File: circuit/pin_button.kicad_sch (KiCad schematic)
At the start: 5 parts, among them SW1 select, SW2 start

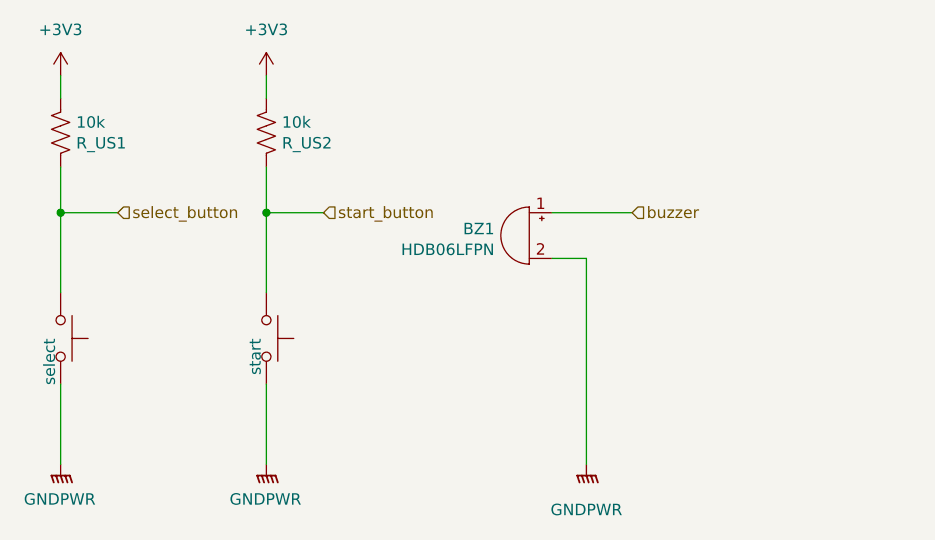
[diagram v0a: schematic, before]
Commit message: [update] update buzzer peripheral circuit
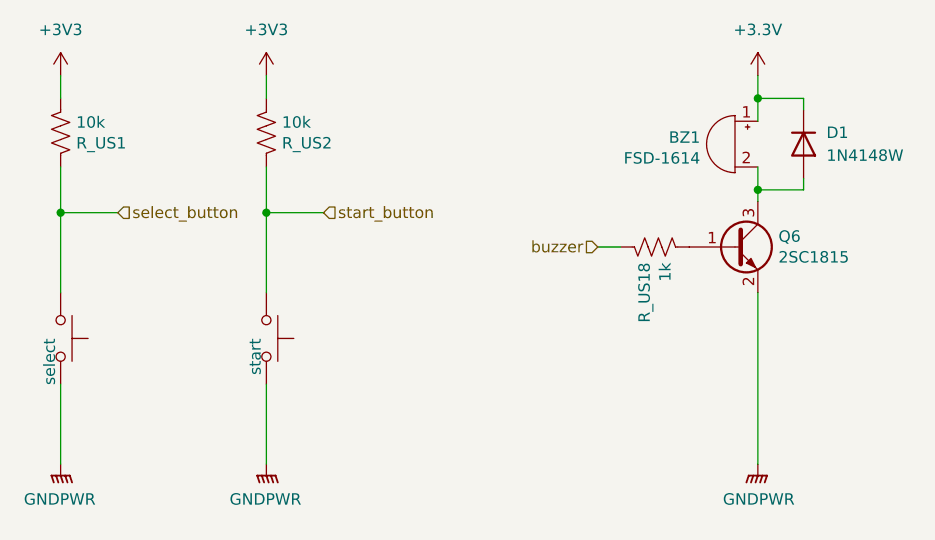
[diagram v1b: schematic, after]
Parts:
- added D1: 1N4148W, Diode_SMD:D_SOD-123, symbol Diode:1N4148W
- added Q6: 2SC1815, Package_TO_SOT_SMD:SOT-23, symbol Transistor_BJT:2SC1815
- added R_US18: 1k, Resistor_SMD:R_0805_2012Metric, symbol Device:R_US
- BZ1: value HDB06LFPN -> FSD-1614
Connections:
- net GNDPWR: now also Q6.2 (E); no longer BZ1.2 (+)
- net buzzer: now also R_US18.1; no longer BZ1.1 (-)
- new net: BZ1.2 (+), D1.2 (A), Q6.3 (C)
- new net: Q6.1 (B), R_US18.2
- new net +3.3V: BZ1.1 (-), D1.1 (K)
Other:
- moved on the sheet: BZ1

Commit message: [update] re-annotate symbols
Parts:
- renumbered Q6 to Q5, R_US1 to R_US16, R_US2 to R_US17, SW1 to SW2, SW2 to SW3
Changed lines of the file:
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@@
 		(dnp no)
 		(fields_autoplaced yes)
-		(property "Reference" "#PWR01"
+		(property "Reference" "#PWR018"
 			(at 116.84 73.66 0)
 			(effects
@@
 			(project "gen3"
 				(path "/4fc99a72-ed0b-4d28-88d8-569af68d8cfc/a6a603d2-5a16-46d3-94ac-e9e8583c5e5b"
-					(reference "#PWR01")
+					(reference "#PWR018")
 					(unit 1)
 				)
@@
 		(on_board yes)
 		(dnp no)
-		(property "Reference" "#PWR03"
+		(property "Reference" "#PWR021"
 			(at 116.84 118.11 0)
 			(effects
@@
 			(project "gen3"
 				(path "/4fc99a72-ed0b-4d28-88d8-569af68d8cfc/a6a603d2-5a16-46d3-94ac-e9e8583c5e5b"
-					(reference "#PWR03")
+					(reference "#PWR021")
 					(unit 1)
 				)
@@
 		(on_board yes)
 		(dnp no)
-		(property "Reference" "#PWR04"
+		(property "Reference" "#PWR022"
 			(at 139.7 118.11 0)
 			(effects
@@
 			(project "gen3"
 				(path "/4fc99a72-ed0b-4d28-88d8-569af68d8cfc/a6a603d2-5a16-46d3-94ac-e9e8583c5e5b"
-					(reference "#PWR04")
+					(reference "#PWR022")
 					(unit 1)
 				)
@@
 		(on_board yes)
 		(dnp no)
-		(property "Reference" "R_US1"
+		(property "Reference" "R_US16"
 			(at 118.5672 77.3684 0)
 			(effects
@@
 			(project "gen3"
 				(path "/4fc99a72-ed0b-4d28-88d8-569af68d8cfc/a6a603d2-5a16-46d3-94ac-e9e8583c5e5b"
-					(reference "R_US1")
+					(reference "R_US16")
 					(unit 1)
 				)
@@
 		(dnp no)
 		(fields_autoplaced yes)
-		(property "Reference" "#PWR02"
+		(property "Reference" "#PWR019"
 			(at 139.7 73.66 0)
 			(effects
@@
 			(project "gen3"
 				(path "/4fc99a72-ed0b-4d28-88d8-569af68d8cfc/a6a603d2-5a16-46d3-94ac-e9e8583c5e5b"
-					(reference "#PWR02")
+					(reference "#PWR019")
 					(unit 1)
 				)
@@
 		(on_board yes)
 		(dnp no)
-		(property "Reference" "Q6"
+		(property "Reference" "Q5"
 			(at 196.596 87.7316 0)
 			(effects
@@
 			(project "gen3"
 				(path "/4fc99a72-ed0b-4d28-88d8-569af68d8cfc/a6a603d2-5a16-46d3-94ac-e9e8583c5e5b"
-					(reference "Q6")
+					(reference "Q5")
 					(unit 1)
 				)
@@
 		(on_board yes)
 		(dnp no)
-		(property "Reference" "#PWR024"
+		(property "Reference" "#PWR023"
 			(at 194.31 118.11 0)
 			(effects
@@
 			(project "gen3"
 				(path "/4fc99a72-ed0b-4d28-88d8-569af68d8cfc/a6a603d2-5a16-46d3-94ac-e9e8583c5e5b"
-					(reference "#PWR024")
+					(reference "#PWR023")
 					(unit 1)
 				)
@@
 		(on_board yes)
 		(dnp no)
-		(property "Reference" "SW2"
+		(property "Reference" "SW3"
 			(at 146.939 99.06 0)
 			(effects
@@
 			(project "gen3"
 				(path "/4fc99a72-ed0b-4d28-88d8-569af68d8cfc/a6a603d2-5a16-46d3-94ac-e9e8583c5e5b"
-					(reference "SW2")
+					(reference "SW3")
 					(unit 1)
 				)
@@
 		(on_board yes)
 		(dnp no)
-		(property "Reference" "R_US2"
+		(property "Reference" "R_US17"
 			(at 141.4272 77.3684 0)
 			(effects
@@
 			(project "gen3"
 				(path "/4fc99a72-ed0b-4d28-88d8-569af68d8cfc/a6a603d2-5a16-46d3-94ac-e9e8583c5e5b"
-					(reference "R_US2")
+					(reference "R_US17")
 					(unit 1)
 				)
@@
 		(dnp no)
 		(fields_autoplaced yes)
-		(property "Reference" "#PWR05"
+		(property "Reference" "#PWR020"
 			(at 194.31 73.66 0)
 			(effects
@@
 			(project ""
 				(path "/4fc99a72-ed0b-4d28-88d8-569af68d8cfc/a6a603d2-5a16-46d3-94ac-e9e8583c5e5b"
-					(reference "#PWR05")
+					(reference "#PWR020")
 					(unit 1)
 				)
@@
 		(on_board yes)
 		(dnp no)
-		(property "Reference" "SW1"
+		(property "Reference" "SW2"
 			(at 124.079 99.06 0)
 			(effects
@@
 			(project "gen3"
 				(path "/4fc99a72-ed0b-4d28-88d8-569af68d8cfc/a6a603d2-5a16-46d3-94ac-e9e8583c5e5b"
-					(reference "SW1")
-					(unit 1)
-				)
+					(reference "SW2")
+					(unit 1)
+				)

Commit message: [wip][add] init pcb data
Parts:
- SW2: footprint Button_Switch_SMD:SW_SPST_PTS645 -> Button_Switch_SMD:SW_SPST_TS-1088-xR020
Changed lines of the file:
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@@
+	)
+	(junction
+		(at 194.31 71.12)
+		(diameter 0)
+		(color 0 0 0 0)
 	)
 	(junction
@@
 	(wire
 		(pts
+			(xy 201.93 69.85) (xy 201.93 71.12)
+		)
+		(stroke
+			(width 0)
+			(type default)
+		)
+	)
+	(wire
+		(pts
 			(xy 116.84 85.09) (xy 116.84 93.98)
 		)
@@
 	(wire
 		(pts
-			(xy 194.31 69.85) (xy 194.31 72.39)
+			(xy 194.31 69.85) (xy 194.31 71.12)
 		)
 		(stroke
@@
 	(wire
 		(pts
+			(xy 194.31 71.12) (xy 194.31 72.39)
+		)
+		(stroke
+			(width 0)
+			(type default)
+		)
+	)
+	(wire
+		(pts
 			(xy 194.31 82.55) (xy 194.31 83.82)
 		)
@@
 		(pts
 			(xy 176.53 88.9) (xy 179.07 88.9)
+		)
+		(stroke
+			(width 0)
+			(type default)
+		)
+	)
+	(wire
+		(pts
+			(xy 201.93 71.12) (xy 194.31 71.12)
 		)
 		(stroke
@@
 	)
 	(symbol
+		(lib_id "power:PWR_FLAG")
+		(at 201.93 69.85 0)
+		(unit 1)
+		(exclude_from_sim no)
+		(in_bom yes)
+		(on_board yes)
+		(dnp no)
+		(fields_autoplaced yes)
+		(property "Reference" "#FLG04"
+			(at 201.93 67.945 0)
+			(effects
+				(font
+					(size 1.27 1.27)
+				)
+				(hide yes)
+			)
+		)
+		(property "Value" "PWR_FLAG"
+			(at 201.93 64.77 0)
+			(effects
+				(font
+					(size 1.27 1.27)
+				)
+			)
+		)
+		(property "Footprint" ""
+			(at 201.93 69.85 0)
+			(effects
+				(font
+					(size 1.27 1.27)
+				)
+				(hide yes)
+			)
+		)
+		(property "Datasheet" "~"
+			(at 201.93 69.85 0)
+			(effects
+				(font
+					(size 1.27 1.27)
+				)
+				(hide yes)
+			)
+		)
+		(property "Description" "Special symbol for telling ERC where power comes from"
+			(at 201.93 69.85 0)
+			(effects
+				(font
+					(size 1.27 1.27)
+				)
+				(hide yes)
+			)
+		)
+		(pin "1"
+		)
+		(instances
+			(project ""
+				(path "/4fc99a72-ed0b-4d28-88d8-569af68d8cfc/a6a603d2-5a16-46d3-94ac-e9e8583c5e5b"
+					(reference "#FLG04")
+					(unit 1)
+				)
+			)
+		)
+	)
+	(symbol
 		(lib_id "Device:R_US")
 		(at 116.84 76.2 0)
@@
 			)
 		)
-		(property "Footprint" "Button_Switch_SMD:SW_SPST_PTS645"
+		(property "Footprint" "Button_Switch_SMD:SW_SPST_TS-1088-xR020"
 			(at 121.92 99.06 0)
 			(effects

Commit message: [!][fix] fix routing 3v3 signal
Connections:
- net +3.3V is gone; now on net +3V3: BZ1.1 (-), D1.1 (K)
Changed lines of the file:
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@@
+	)
+	(symbol
+		(lib_id "power:+3V3")
+		(at 194.31 69.85 0)
+		(unit 1)
+		(exclude_from_sim no)
+		(in_bom yes)
+		(on_board yes)
+		(dnp no)
+		(fields_autoplaced yes)
+		(property "Reference" "#PWR020"
+			(at 194.31 73.66 0)
+			(effects
+				(font
+					(size 1.27 1.27)
+				)
+				(hide yes)
+			)
+		)
+		(property "Value" "+3V3"
+			(at 194.31 64.77 0)
+			(effects
+				(font
+					(size 1.27 1.27)
+				)
+			)
+		)
+		(property "Footprint" ""
+			(at 194.31 69.85 0)
+			(effects
+				(font
+					(size 1.27 1.27)
+				)
+				(hide yes)
+			)
+		)
+		(property "Datasheet" ""
+			(at 194.31 69.85 0)
+			(effects
+				(font
+					(size 1.27 1.27)
+				)
+				(hide yes)
+			)
+		)
+		(property "Description" "Power symbol creates a global label with name \"+3V3\""
+			(at 194.31 69.85 0)
+			(effects
+				(font
+					(size 1.27 1.27)
+				)
+				(hide yes)
+			)
+		)
+		(pin "1"
+		)
+		(instances
+			(project ""
+				(path "/4fc99a72-ed0b-4d28-88d8-569af68d8cfc/a6a603d2-5a16-46d3-94ac-e9e8583c5e5b"
+					(reference "#PWR020")
+					(unit 1)
+				)
+			)
+		)
 	)
 	(symbol
@@
 					(unit 1)
 				)
-			)
-		)
-	)
-	(symbol
-		(lib_id "power:+3.3V")
-		(at 194.31 69.85 0)
-		(unit 1)
-		(exclude_from_sim no)
-		(in_bom yes)
-		(on_board yes)
-		(dnp no)
-		(fields_autoplaced yes)
-		(property "Reference" "#PWR020"
-			(at 194.31 73.66 0)
-			(effects
-				(font
-					(size 1.27 1.27)
-				)
-				(hide yes)
-			)
-		)
-		(property "Value" "+3.3V"
-			(at 194.31 64.77 0)
-			(effects
-				(font
-					(size 1.27 1.27)
-				)
-			)
-		)
-		(property "Footprint" ""
-			(at 194.31 69.85 0)
-			(effects
-				(font
-					(size 1.27 1.27)
-				)
-				(hide yes)
-			)
-		)
-		(property "Datasheet" ""
-			(at 194.31 69.85 0)
-			(effects
-				(font
-					(size 1.27 1.27)
-				)
-				(hide yes)
-			)
-		)
-		(property "Description" "Power symbol creates a global label with name \"+3.3V\""
-			(at 194.31 69.85 0)
-			(effects
-				(font
-					(size 1.27 1.27)
-				)
-				(hide yes)
-			)
-		)
-		(pin "1"
-		)
-		(instances
-			(project ""
-				(path "/4fc99a72-ed0b-4d28-88d8-569af68d8cfc/a6a603d2-5a16-46d3-94ac-e9e8583c5e5b"
-					(reference "#PWR020")
-					(unit 1)
-				)
